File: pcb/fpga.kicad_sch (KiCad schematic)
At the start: 30 parts

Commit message: pcb: start fpga
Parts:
- added U? (x5): XC7A75T-CSG324, Package_BGA:Xilinx_CSG324, symbol FPGA_Xilinx_Artix7:XC7A75T-CSG324
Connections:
- net +1V0: now also U?.F10 (VCCBRAM), U?.F8 (VCCINT), U?.G11 (VCCBRAM), U?.G7 (VCCINT), U?.G9 (VCCINT), U?.H8 (VCCINT), U?.J11 (VCCINT), U?.J7 (VCCINT), U?.K8 (VCCINT), U?.L11 (VCCINT), U?.L7 (VCCINT), U?.M10 (VCCINT), U?.M8 (VCCINT), U?.N11 (VCCINT), U?.N7 (VCCINT), U?.N9 (VCCINT)
- net +1V8: now also U?.F12 (VCCAUX), U?.H12 (VCCAUX), U?.K12 (VCCAUX), U?.M12 (VCCAUX)
- net +3V3: now also U?.A17 (VCCO_15), U?.B10 (VCCO_16), U?.C13 (VCCO_15), U?.D16 (VCCO_15), U?.G15 (VCCO_15), U?.H18 (VCCO_15), U?.K14 (VCCO_15), U?.L17 (VCCO_14), U?.N13 (VCCO_14), U?.P16 (VCCO_14), U?.R9 (VCCO_0), U?.T12 (VCCO_14), U?.U15 (VCCO_14), U?.V18 (VCCO_14)
- net GND: now also U?.A12 (GND), U?.A2 (GND), U?.A7 (VCCO_35), U?.B15 (GND), U?.B5 (GND), U?.C18 (GND), U?.C3 (VCCO_35), U?.C8 (GND), U?.D1 (GND), U?.D11 (GND), U?.D6 (VCCO_35), U?.E14 (GND), U?.E4 (GND), U?.E8 (VCCBATT_0), U?.F11 (GND), U?.F17 (GND), U?.F2 (VCCO_35), U?.F7 (GND), U?.F9 (GND), U?.G10 (GND), U?.G12 (GND), U?.G5 (VCCO_35), U?.G8 (GND), U?.H10 (VCCADC_0), U?.H11 (GND), U?.H13 (GND), U?.H3 (GND), U?.H7 (GND), U?.H9 (GNDADC_0), U?.J1 (VCCO_35), U?.J12 (GND), U?.J16 (GND), U?.J6 (GND), U?.J8 (GND), U?.K11 (GND), U?.K4 (VCCO_34), U?.K7 (GND), U?.L12 (GND), U?.L15 (IO_L3P_T0_DQS_PUDC_B_14), U?.L2 (GND), U?.L8 (GND), U?.M11 (GND), U?.M15 (GND), U?.M5 (GND), U?.M7 (GND), U?.M9 (GND), U?.N10 (GND), U?.N12 (GND), U?.N18 (GND), U?.N3 (VCCO_34), U?.N8 (GND), U?.P1 (GND), U?.P6 (VCCO_34), U?.R14 (GND), U?.R4 (GND), U?.T17 (GND), U?.T2 (VCCO_34), U?.T7 (GND), U?.U10 (GND), U?.U5 (VCCO_34), U?.V13 (GND), U?.V3 (GND), U?.V8 (VCCO_34)
- net at Y?.3 (OUT): now also U?.P15 (IO_L13P_T2_MRCC_14)
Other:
- note added: "*obs"
- note added: "sram"
- moved on the sheet: C82

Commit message: pcb: add sram and flash to fpga
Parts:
- added C?: 100n, symbol Device:C
- added J?: Conn_ST_STDC14, symbol Connector:Conn_ST_STDC14
- added R? (x2): 4.7k, symbol Device:R
- added R?: 2.4k, symbol Device:R
- added U?: S70KS1283GABHB023, S70KS1283GABHB023:BGA24C100P5X5_600X800X100, symbol S70KS1283GABHB023:S70KS1283GABHB023
- added U?: W25Q128JVS, Package_SO:SOIC-8_5.3x5.3mm_P1.27mm, symbol Memory_Flash:W25Q128JVS
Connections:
- net +1V8: now also U?.B4 (VCC), U?.D1 (VCCQ), U?.E4 (VCCQ)
- net +3V3: now also C?.2, R?.1, R?.1, R?.1, U?.8 (VCC)
- net GND: now also C?.1, U?.4 (GND), U?.B1 (CK_N), U?.B3 (VSS), U?.C1 (VSSQ), U?.C2 (RFU4), U?.E5 (VSSQ)
- net at U?.K17 (IO_L1P_T0_D00_MOSI_14): now also U?.5 (DI/IO_{0})
- net at U?.K18 (IO_L1N_T0_D01_DIN_14): now also U?.2 (DO/IO_{1})
- net at U?.L13 (IO_L6P_T0_FCS_B_14): now also R?.2, U?.1 (~{CS})
- net at U?.L14 (IO_L2P_T0_D02_14): now also R?.2, U?.3 (~{WP}/IO_{2})
- net at U?.M14 (IO_L2N_T0_D03_14): now also R?.2, U?.7 (~{HOLD}/~{RESET}/IO_{3})
- net at U?.E9 (CCLK_0): now also U?.6 (CLK), U?.A2 (RFU1), U?.B2 (CK)
- new net: J?.5 (GND), J?.7 (GND)
- no-connect marks 0 -> 3
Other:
- note added: "PCK"
- note added: "PCK_N"
- note removed: "*obs"
- note removed: "sram"
- moved on the sheet: U?D

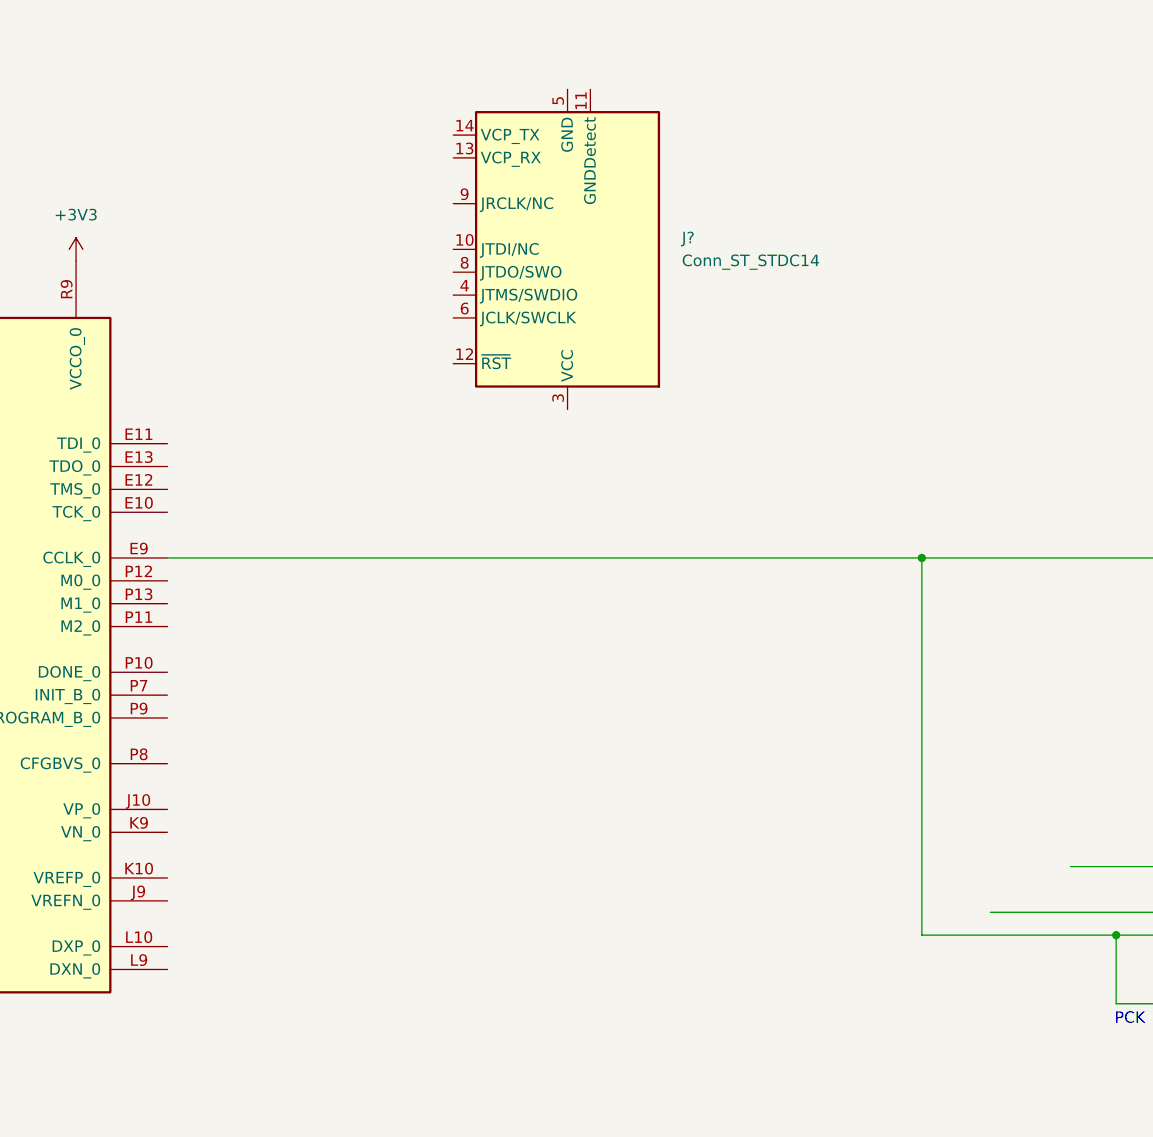
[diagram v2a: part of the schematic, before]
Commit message: pcb/fpga: add jtag
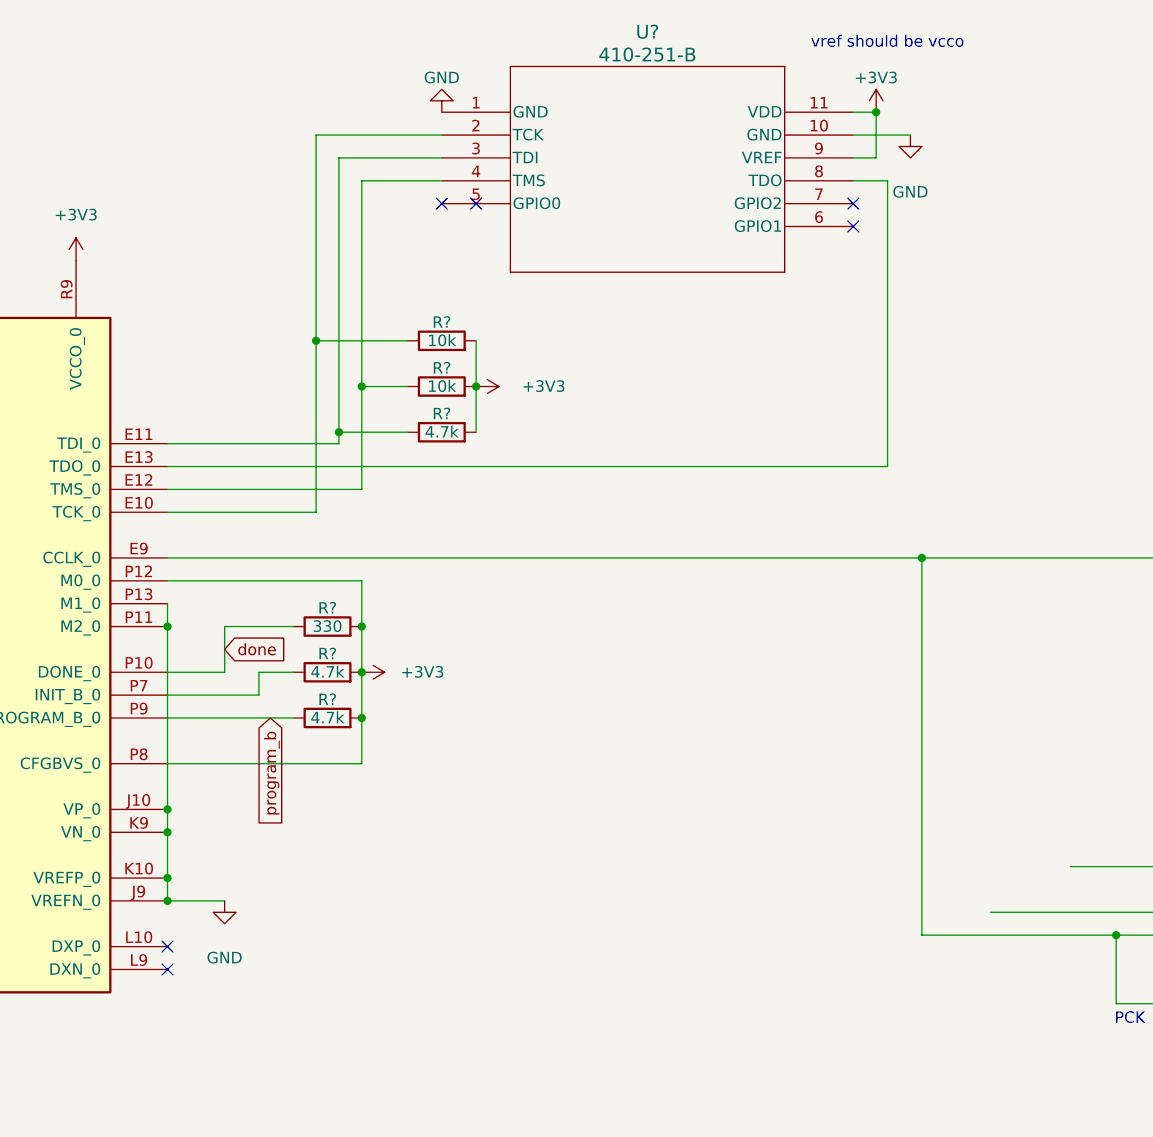
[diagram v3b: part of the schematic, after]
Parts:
- removed J?: Conn_ST_STDC14, symbol Connector:Conn_ST_STDC14
- added R? (x2): 10k, symbol Device:R
- added R? (x3): 4.7k, symbol Device:R
- added R?: 330, symbol Device:R
- added U?: 410-251-B, IC11_410-251-B_DGT, symbol 2026-09-16_13-52-00:410-251-B
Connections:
- net +3V3: now also U?.P12 (M0_0), U?.P8 (CFGBVS_0), R?.2, R?.2, R?.2, R?.2, R?.2, R?.2, U?.11 (VDD), U?.9 (VREF)
- net GND: now also U?.J10 (VP_0), U?.J9 (VREFN_0), U?.K10 (VREFP_0), U?.K9 (VN_0), U?.P11 (M2_0), U?.P13 (M1_0), U?.1 (GND), U?.10 (GND)
- net at U?.E10 (TCK_0): now also R?.1, U?.2 (TCK)
- net at U?.E11 (TDI_0): now also R?.1, U?.3 (TDI)
- net at U?.E12 (TMS_0): now also R?.1, U?.4 (TMS)
- net at U?.E13 (TDO_0): now also U?.8 (TDO)
- net done: now reaches U?.P10 (DONE_0)
- net done: now also R?.1
- net at U?.P7 (INIT_B_0): now also R?.1
- net program_b: now reaches U?.P9 (PROGRAM_B_0)
- net program_b: now also R?.1
- no-connect marks 3 -> 9
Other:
- note added: "vref should be vcco"

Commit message: pcb/fpga: change sram module to 3v3
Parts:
- removed U?: S70KS1283GABHB023, S70KS1283GABHB023:BGA24C100P5X5_600X800X100, symbol S70KS1283GABHB023:S70KS1283GABHB023
- added R?: 4.7k, symbol Device:R
- added U?: S70KL1283GABHI020, symbol S70KL1283GABHI020:S70KL1283GABHI020
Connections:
- net +3V3: now also R?.2, U?.B4 (VCC), U?.D1 (VCCQ), U?.E4 (VCCQ); no longer U?.P12 (M0_0)
- net GND: now also U?.B1 (CK_N), U?.B3 (VSS), U?.C1 (VSSQ), U?.E5 (VSSQ)
- net at U?.T10 (IO_L24N_T3_A00_D16_14): now also U?.A4 (RESET_N)
- net at U?.T11 (IO_L19P_T3_A10_D26_14): now also U?.D3 (DQ0)
- net at U?.T13 (IO_L23P_T3_A03_D19_14): now also U?.E2 (DQ6)
- net at U?.T9 (IO_L24P_T3_A01_D17_14): now also U?.C3 (RWDS)
- net at U?.U11 (IO_L19N_T3_A09_D25_VREF_14): now also U?.D2 (DQ1)
- net at U?.U12 (IO_L20P_T3_A08_D24_14): now also U?.C4 (DQ2)
- net at U?.U13 (IO_L23N_T3_A02_D18_14): now also U?.E1 (DQ7)
- net at U?.U14 (IO_L22P_T3_A05_D21_14): now also U?.D5 (DQ4)
- net at U?.V10 (IO_L21P_T3_DQS_14): now also U?.B2 (CK)
- net at U?.V11 (IO_L21N_T3_DQS_A06_D22_14): now also U?.A3 (CS_N)
- net at U?.V12 (IO_L20N_T3_A07_D23_14): now also U?.D4 (DQ3)
- net at U?.V14 (IO_L22N_T3_A04_D20_14): now also U?.E3 (DQ5)
- new net: R?.1, U?.P12 (M0_0)
- no-connect marks 9 -> 6
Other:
- note removed: "PCK"
- note removed: "PCK_N"

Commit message: pcb/fpga: change 75tcsg to 50tftg
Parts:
- removed U? (x5): XC7A75T-CSG324, Package_BGA:Xilinx_CSG324, symbol FPGA_Xilinx_Artix7:XC7A75T-CSG324
- added U? (x4): XC7A50T-FTG256, Package_BGA:Xilinx_FTG256, symbol FPGA_Xilinx_Artix7:XC7A50T-FTG256
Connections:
- net +1V0: now also U?.E10 (VCCBRAM), U?.F11 (VCCBRAM), U?.F7 (VCCINT), U?.F9 (VCCINT), U?.G6 (VCCINT), U?.H9 (VCCINT), U?.J6 (VCCINT), U?.K9 (VCCINT), U?.L8 (VCCINT)
- net +1V8: now also U?.G10 (VCCAUX), U?.J10 (VCCAUX), U?.K11 (VCCAUX), U?.L10 (VCCAUX)
- net +3V3: now also U?.A16 (VCCO_15), U?.B13 (VCCO_15), U?.C10 (VCCO_15), U?.E14 (VCCO_15), U?.E7 (CFGBVS_0), U?.H15 (VCCO_15), U?.J12 (VCCO_15), U?.L16 (VCCO_14), U?.L6 (VCCO_0), U?.M13 (VCCO_14), U?.N10 (VCCO_14), U?.P7 (VCCO_14), U?.R14 (VCCO_14), U?.T11 (VCCO_14)
- net GND: now also U?.A1 (GND), U?.A11 (GND), U?.A6 (VCCO_35), U?.B3 (VCCO_35), U?.B8 (GND), U?.C15 (GND), U?.C5 (GND), U?.D12 (GND), U?.D2 (GND), U?.D7 (VCCO_35), U?.E4 (VCCO_35), U?.E9 (GND), U?.F1 (VCCO_35), U?.F10 (GND), U?.F16 (GND), U?.F6 (GND), U?.F8 (VCCBATT_0), U?.G13 (GND), U?.G3 (GND), U?.G7 (GNDADC_0), U?.G8 (VCCADC_0), U?.G9 (GND), U?.H6 (GND), U?.H7 (VREFN_0), U?.H8 (VP_0), U?.J11 (GND), U?.J2 (VCCO_35), U?.J7 (VN_0), U?.J8 (VREFP_0), U?.J9 (GND), U?.K14 (GND), U?.K4 (GND), U?.K6 (GND), U?.L1 (GND), U?.L11 (GND), U?.L15 (IO_L3P_T0_DQS_PUDC_B_14), U?.M10 (M1_0), U?.M11 (M2_0), U?.M3 (VCCO_34), U?.M8 (GND), U?.N15 (GND), U?.N5 (GND), U?.P12 (GND), U?.P2 (GND), U?.R4 (VCCO_34), U?.R9 (GND), U?.T1 (VCCO_34), U?.T16 (GND), U?.T6 (GND)
- net done: now also U?.H10 (DONE_0)
- net program_b: now also U?.L9 (PROGRAM_B_0)
- net at R?.1: now also U?.M9 (M0_0)
- net at R?.2, U?.3 (~{WP}/IO_{2}): now also U?.K15 (IO_L2P_T0_D02_14)
- net at R?.1, U?.4 (TMS): now also U?.M7 (TMS_0)
- net at R?.2, U?.1 (~{CS}): now also U?.L12 (IO_L6P_T0_FCS_B_14)
- net at R?.1, U?.3 (TDI): now also U?.N7 (TDI_0)
- net at R?.1, U?.2 (TCK): now also U?.L7 (TCK_0)
- net at R?.1: now also U?.K10 (INIT_B_0)
- net at R?.2, U?.7 (~{HOLD}/~{RESET}/IO_{3}): now also U?.K16 (IO_L2N_T0_D03_14)
- net at U?.5 (DI/IO_{0}): now also U?.J13 (IO_L1P_T0_D00_MOSI_14)
- net at U?.2 (DO/IO_{1}): now also U?.J14 (IO_L1N_T0_D01_DIN_14)
- net at Y?.3 (OUT): now also U?.N11 (IO_L13P_T2_MRCC_14)
- net at U?.A4 (RESET_N): now also U?.R7 (IO_L24N_T3_A00_D16_14)
- net at U?.D3 (DQ0): now also U?.M6 (IO_L19P_T3_A10_D26_14)
- net at U?.E2 (DQ6): now also U?.R5 (IO_L23P_T3_A03_D19_14)
- net at U?.C3 (RWDS): now also U?.R6 (IO_L24P_T3_A01_D17_14)
- net at U?.D2 (DQ1): now also U?.N6 (IO_L19N_T3_A09_D25_VREF_14)
- net at U?.C4 (DQ2): now also U?.P8 (IO_L20P_T3_A08_D24_14)
- net at U?.E1 (DQ7): now also U?.T5 (IO_L23N_T3_A02_D18_14)
- net at U?.D5 (DQ4): now also U?.T9 (IO_L22P_T3_A05_D21_14)
- net at U?.B2 (CK): now also U?.T7 (IO_L21P_T3_DQS_14)
- net at U?.A3 (CS_N): now also U?.T8 (IO_L21N_T3_DQS_A06_D22_14)
- net at U?.D4 (DQ3): now also U?.R8 (IO_L20N_T3_A07_D23_14)
- net at U?.E3 (DQ5): now also U?.T10 (IO_L22N_T3_A04_D20_14)
- net at U?.6 (CLK): now also U?.E8 (CCLK_0)
- net at U?.8 (TDO): now also U?.N8 (TDO_0)
